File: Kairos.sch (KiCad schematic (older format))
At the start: 37 parts, among them U1 ATMEGA32U2-AU

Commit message: LED portion of main matrix, bug fixes
Add junctions which need to exist
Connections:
- net LEDGND: now reaches Q?.2 (C)
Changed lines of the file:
@@
 	0    1    1    0
 $EndComp
+Wire Wire Line
+	3850 1400 3850 1500
+Text GLabel 3850 1500 0    60   Input ~ 0
+LEDGND
 $EndSCHEMATC

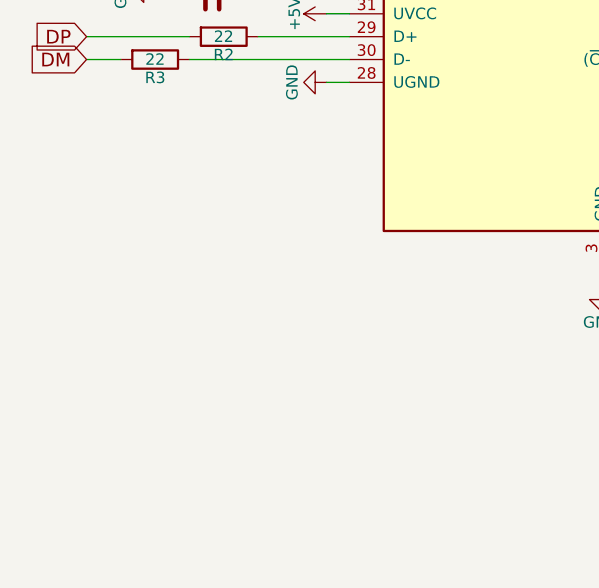
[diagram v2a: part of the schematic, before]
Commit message: Add USB
USB connector and PTC fuse for 5V
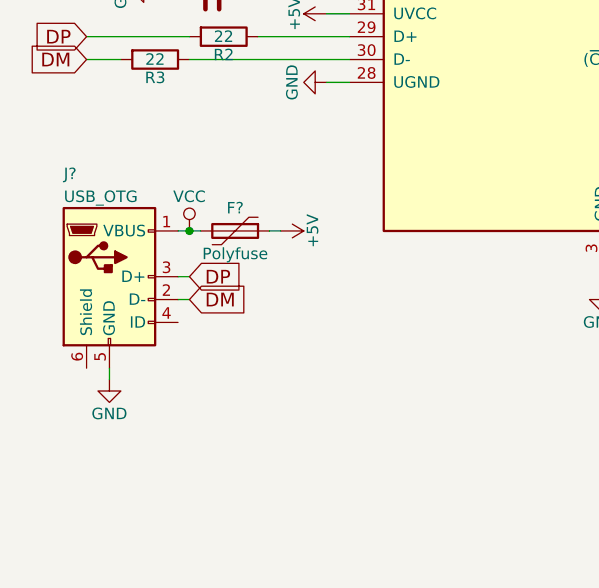
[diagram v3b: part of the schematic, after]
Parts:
- added F?: Polyfuse, symbol Polyfuse
- added J?: USB_OTG, symbol USB_OTG
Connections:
- net +5V: now also F?.1
- net DM: now also J?.2 (D-)
- net DP: now also J?.3 (D+)
- net GND: now also J?.5 (GND)
- new net VCC: F?.2, J?.1 (VBUS)
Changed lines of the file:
@@
 Text GLabel 3850 1500 0    60   Input ~ 0
 LEDGND
+$Comp
+L USB_OTG J?
+U 1 1 594639AC
+P 900 4500
+F 0 "J?" H 700 4950 50  0000 L CNN
+F 1 "USB_OTG" H 700 4850 50  0000 L CNN
+F 2 "" H 1050 4450 50  0001 C CNN
+F 3 "" H 1050 4450 50  0001 C CNN
+	1    900  4500
+	1    0    0    -1
+$EndComp
+$Comp
+L VCC #PWR?
+U 1 1 59465485
+P 1250 4300
+F 0 "#PWR?" H 1250 4150 50  0001 C CNN
+F 1 "VCC" H 1250 4450 50  0000 C CNN
+F 2 "" H 1250 4300 50  0001 C CNN
+F 3 "" H 1250 4300 50  0001 C CNN
+	1    1250 4300
+	1    0    0    -1
+$EndComp
+Wire Wire Line
+	1200 4300 1300 4300
+$Comp
+L Polyfuse F?
+U 1 1 5946558C
+P 1450 4300
+F 0 "F?" V 1350 4300 50  0000 C CNN
+F 1 "Polyfuse" V 1550 4300 50  0000 C CNN
+F 2 "" H 1500 4100 50  0001 L CNN
+F 3 "" H 1450 4300 50  0001 C CNN
+	1    1450 4300
+	0    1    1    0
+$EndComp
+Connection ~ 1250 4300
+Wire Wire Line
+	1600 4300 1650 4300
+$Comp
+L +5V #PWR?
+U 1 1 59465754
+P 1650 4300
+F 0 "#PWR?" H 1650 4150 50  0001 C CNN
+F 1 "+5V" H 1650 4440 50  0000 C CNN
+F 2 "" H 1650 4300 50  0001 C CNN
+F 3 "" H 1650 4300 50  0001 C CNN
+	1    1650 4300
+	0    1    1    0
+$EndComp
+Wire Wire Line
+	1200 4500 1250 4500
+Wire Wire Line
+	1200 4600 1250 4600
+Wire Wire Line
+	900  4900 900  4950
+$Comp
+L GND #PWR?
+U 1 1 594659E2
+P 900 4950
+F 0 "#PWR?" H 900 4700 50  0001 C CNN
+F 1 "GND" H 900 4800 50  0000 C CNN
+F 2 "" H 900 4950 50  0001 C CNN
+F 3 "" H 900 4950 50  0001 C CNN
+	1    900  4950
+	1    0    0    -1
+$EndComp
+Text GLabel 1250 4500 2    60   Input ~ 0
+DP
+Text GLabel 1250 4600 2    60   Input ~ 0
+DM
 $EndSCHEMATC

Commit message: Update annotations
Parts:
- gave numbers to parts that had none: 15
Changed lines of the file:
@@
 $EndComp
 $Comp
-L GND #PWR?
+L GND #PWR01
 U 1 1 5918DBD0
 P 1100 3250
-F 0 "#PWR?" H 1100 3000 50  0001 C CNN
+F 0 "#PWR01" H 1100 3000 50  0001 C CNN
 F 1 "GND" H 1100 3100 50  0000 C CNN
 F 2 "" H 1100 3250 50  0001 C CNN
@@
 $EndComp
 $Comp
-L +5V #PWR?
+L +5V #PWR02
 U 1 1 5918DF71
 P 1850 3350
-F 0 "#PWR?" H 1850 3200 50  0001 C CNN
+F 0 "#PWR02" H 1850 3200 50  0001 C CNN
 F 1 "+5V" H 1850 3490 50  0000 C CNN
 F 2 "" H 1850 3350 50  0001 C CNN
@@
 $EndComp
 $Comp
-L +5V #PWR?
+L +5V #PWR03
 U 1 1 5918E0B6
 P 1850 2450
-F 0 "#PWR?" H 1850 2300 50  0001 C CNN
+F 0 "#PWR03" H 1850 2300 50  0001 C CNN
 F 1 "+5V" H 1850 2590 50  0000 C CNN
 F 2 "" H 1850 2450 50  0001 C CNN
@@
 $EndComp
 $Comp
-L +5V #PWR?
+L +5V #PWR04
 U 1 1 5918E1F7
 P 3050 1550
-F 0 "#PWR?" H 3050 1400 50  0001 C CNN
+F 0 "#PWR04" H 3050 1400 50  0001 C CNN
 F 1 "+5V" H 3050 1690 50  0000 C CNN
 F 2 "" H 3050 1550 50  0001 C CNN
@@
 $EndComp
 $Comp
-L GND #PWR?
+L GND #PWR05
 U 1 1 5918E4E7
 P 1850 3650
-F 0 "#PWR?" H 1850 3400 50  0001 C CNN
+F 0 "#PWR05" H 1850 3400 50  0001 C CNN
 F 1 "GND" H 1850 3500 50  0000 C CNN
 F 2 "" H 1850 3650 50  0001 C CNN
@@
 $EndComp
 $Comp
-L GND #PWR?
+L GND #PWR06
 U 1 1 5918E5DF
 P 3050 4550
-F 0 "#PWR?" H 3050 4300 50  0001 C CNN
+F 0 "#PWR06" H 3050 4300 50  0001 C CNN
 F 1 "GND" H 3050 4400 50  0000 C CNN
 F 2 "" H 3050 4550 50  0001 C CNN
@@
 $EndComp
 $Comp
-L GND #PWR?
+L GND #PWR07
 U 1 1 5918EBA1
 P 1150 2350
-F 0 "#PWR?" H 1150 2100 50  0001 C CNN
+F 0 "#PWR07" H 1150 2100 50  0001 C CNN
 F 1 "GND" H 1150 2200 50  0000 C CNN
 F 2 "" H 1150 2350 50  0001 C CNN
@@
 $EndComp
 $Comp
-L GND #PWR?
+L GND #PWR08
 U 1 1 5918EEAC
 P 4650 3550
-F 0 "#PWR?" H 4650 3300 50  0001 C CNN
+F 0 "#PWR08" H 4650 3300 50  0001 C CNN
 F 1 "GND" H 4650 3400 50  0000 C CNN
 F 2 "" H 4650 3550 50  0001 C CNN
@@
 $EndComp
 $Comp
-L +5V #PWR?
+L +5V #PWR09
 U 1 1 5919016B
 P 1350 1500
-F 0 "#PWR?" H 1350 1350 50  0001 C CNN
+F 0 "#PWR09" H 1350 1350 50  0001 C CNN
 F 1 "+5V" H 1350 1640 50  0000 C CNN
 F 2 "" H 1350 1500 50  0001 C CNN
@@
 $EndComp
 $Comp
-L GND #PWR?
+L GND #PWR010
 U 1 1 59190191
 P 1350 2000
-F 0 "#PWR?" H 1350 1750 50  0001 C CNN
+F 0 "#PWR010" H 1350 1750 50  0001 C CNN
 F 1 "GND" H 1350 1850 50  0000 C CNN
 F 2 "" H 1350 2000 50  0001 C CNN
@@
 $EndComp
 $Comp
-L GND #PWR?
+L GND #PWR011
 U 1 1 59191048
 P 750 2700
-F 0 "#PWR?" H 750 2450 50  0001 C CNN
+F 0 "#PWR011" H 750 2450 50  0001 C CNN
 F 1 "GND" H 750 2550 50  0000 C CNN
 F 2 "" H 750 2700 50  0001 C CNN
@@
 $EndComp
 $Comp
-L BCP51 Q?
+L BCP51 Q1
 U 1 1 591916D1
 P 3950 1200
-F 0 "Q?" H 4150 1275 50  0000 L CNN
+F 0 "Q1" H 4150 1275 50  0000 L CNN
 F 1 "NSS40301MZ4T1G" H 4150 1200 50  0000 L CNN
 F 2 "TO_SOT_Packages_SMD:SOT-223" H 4150 1125 50  0001 L CIN
@@
 $EndComp
 $Comp
-L GND #PWR?
+L GND #PWR012
 U 1 1 59191F20
 P 3850 900
-F 0 "#PWR?" H 3850 650 50  0001 C CNN
+F 0 "#PWR012" H 3850 650 50  0001 C CNN
 F 1 "GND" H 3850 750 50  0000 C CNN
 F 2 "" H 3850 900 50  0001 C CNN
@@
 $EndComp
 $Comp
-L +5V #PWR?
+L +5V #PWR013
 U 1 1 59196108
 P 8500 850
-F 0 "#PWR?" H 8500 700 50  0001 C CNN
+F 0 "#PWR013" H 8500 700 50  0001 C CNN
 F 1 "+5V" H 8500 990 50  0000 C CNN
 F 2 "" H 8500 850 50  0001 C CNN
@@
 $EndComp
 $Comp
-L GND #PWR?
+L GND #PWR014
 U 1 1 5919672A
 P 9600 850
-F 0 "#PWR?" H 9600 600 50  0001 C CNN
+F 0 "#PWR014" H 9600 600 50  0001 C CNN
 F 1 "GND" H 9600 700 50  0000 C CNN
 F 2 "" H 9600 850 50  0001 C CNN
@@
 	9950 850  9950 5750
 $Comp
-L +5V #PWR?
+L +5V #PWR015
 U 1 1 59197C26
 P 9950 850
-F 0 "#PWR?" H 9950 700 50  0001 C CNN
+F 0 "#PWR015" H 9950 700 50  0001 C CNN
 F 1 "+5V" H 9950 990 50  0000 C CNN
 F 2 "" H 9950 850 50  0001 C CNN
@@
 	11050 1400 11000 1400
 $Comp
-L GND #PWR?
+L GND #PWR016
 U 1 1 591994C3
 P 11050 850
-F 0 "#PWR?" H 11050 600 50  0001 C CNN
+F 0 "#PWR016" H 11050 600 50  0001 C CNN
 F 1 "GND" H 11050 700 50  0000 C CNN
 F 2 "" H 11050 850 50  0001 C CNN
@@
 $EndSheet
 $Comp
-L C CR?
+L C CR1
 U 1 1 5919EB18
 P 6350 5400
-F 0 "CR?" H 6375 5500 50  0000 L CNN
+F 0 "CR1" H 6375 5500 50  0000 L CNN
 F 1 "100nF" H 6375 5300 50  0000 L CNN
 F 2 "" H 6388 5250 50  0001 C CNN
@@
 $EndComp
 $Comp
-L C CR?
+L C CR2
 U 1 1 5919FDAD
 P 6650 5400
-F 0 "CR?" H 6675 5500 50  0000 L CNN
+F 0 "CR2" H 6675 5500 50  0000 L CNN
 F 1 "100nF" H 6675 5300 50  0000 L CNN
 F 2 "" H 6688 5250 50  0001 C CNN
@@
 $EndComp
 $Comp
-L C CR?
+L C CR3
 U 1 1 5919FE22
 P 6950 5400
-F 0 "CR?" H 6975 5500 50  0000 L CNN
+F 0 "CR3" H 6975 5500 50  0000 L CNN
 F 1 "100nF" H 6975 5300 50  0000 L CNN
 F 2 "" H 6988 5250 50  0001 C CNN
@@
 $EndComp
 $Comp
-L C CR?
+L C CR4
 U 1 1 5919FE8E
 P 7250 5400
-F 0 "CR?" H 7275 5500 50  0000 L CNN
+F 0 "CR4" H 7275 5500 50  0000 L CNN
 F 1 "100nF" H 7275 5300 50  0000 L CNN
 F 2 "" H 7288 5250 50  0001 C CNN
@@
 $EndComp
 $Comp
-L C CR?
+L C CR5
 U 1 1 591A01D2
 P 7550 5400
-F 0 "CR?" H 7575 5500 50  0000 L CNN
+F 0 "CR5" H 7575 5500 50  0000 L CNN
 F 1 "100nF" H 7575 5300 50  0000 L CNN
 F 2 "" H 7588 5250 50  0001 C CNN
@@
 $EndComp
 $Comp
-L C CR?
+L C CR6
 U 1 1 591A0284
 P 7850 5400
-F 0 "CR?" H 7875 5500 50  0000 L CNN
+F 0 "CR6" H 7875 5500 50  0000 L CNN
 F 1 "100nF" H 7875 5300 50  0000 L CNN
 F 2 "" H 7888 5250 50  0001 C CNN
@@
 	7850 5550 6200 5550
 $Comp
-L +5V #PWR?
+L +5V #PWR017
 U 1 1 591A0912
 P 6200 5250
-F 0 "#PWR?" H 6200 5100 50  0001 C CNN
+F 0 "#PWR017" H 6200 5100 50  0001 C CNN
 F 1 "+5V" H 6200 5390 50  0000 C CNN
 F 2 "" H 6200 5250 50  0001 C CNN
@@
 $EndComp
 $Comp
-L GND #PWR?
+L GND #PWR018
 U 1 1 591A09A2
 P 6200 5550
-F 0 "#PWR?" H 6200 5300 50  0001 C CNN
+F 0 "#PWR018" H 6200 5300 50  0001 C CNN
 F 1 "GND" H 6200 5400 50  0000 C CNN
 F 2 "" H 6200 5550 50  0001 C CNN
@@
 $EndComp
 $Comp
-L C CR?
+L C CR7
 U 1 1 591A0E23
 P 6350 5900
-F 0 "CR?" H 6375 6000 50  0000 L CNN
+F 0 "CR7" H 6375 6000 50  0000 L CNN
 F 1 "100nF" H 6375 5800 50  0000 L CNN
 F 2 "" H 6388 5750 50  0001 C CNN
@@
 $EndComp
 $Comp
-L C CR?
+L C CR8
 U 1 1 591A0E29
 P 6650 5900
-F 0 "CR?" H 6675 6000 50  0000 L CNN
+F 0 "CR8" H 6675 6000 50  0000 L CNN
 F 1 "100nF" H 6675 5800 50  0000 L CNN
 F 2 "" H 6688 5750 50  0001 C CNN
@@
 $EndComp
 $Comp
-L C CR?
+L C CR9
 U 1 1 591A0E2F
 P 6950 5900
-F 0 "CR?" H 6975 6000 50  0000 L CNN
+F 0 "CR9" H 6975 6000 50  0000 L CNN
 F 1 "100nF" H 6975 5800 50  0000 L CNN
 F 2 "" H 6988 5750 50  0001 C CNN
@@
 $EndComp
 $Comp
-L C CR?
+L C CR10
 U 1 1 591A0E35
 P 7250 5900
-F 0 "CR?" H 7275 6000 50  0000 L CNN
+F 0 "CR10" H 7275 6000 50  0000 L CNN
 F 1 "100nF" H 7275 5800 50  0000 L CNN
 F 2 "" H 7288 5750 50  0001 C CNN
@@
 $EndComp
 $Comp
-L C CR?
+L C CR11
 U 1 1 591A0E3B
 P 7550 5900
-F 0 "CR?" H 7575 6000 50  0000 L CNN
+F 0 "CR11" H 7575 6000 50  0000 L CNN
 F 1 "100nF" H 7575 5800 50  0000 L CNN
 F 2 "" H 7588 5750 50  0001 C CNN
@@
 $EndComp
 $Comp
-L C CR?
+L C CR12
 U 1 1 591A0E41
 P 7850 5900
-F 0 "CR?" H 7875 6000 50  0000 L CNN
+F 0 "CR12" H 7875 6000 50  0000 L CNN
 F 1 "100nF" H 7875 5800 50  0000 L CNN
 F 2 "" H 7888 5750 50  0001 C CNN
@@
 	7850 6050 6200 6050
 $Comp
-L +5V #PWR?
+L +5V #PWR019
 U 1 1 591A0E49
 P 6200 5750
-F 0 "#PWR?" H 6200 5600 50  0001 C CNN
+F 0 "#PWR019" H 6200 5600 50  0001 C CNN
 F 1 "+5V" H 6200 5890 50  0000 C CNN
 F 2 "" H 6200 5750 50  0001 C CNN
@@
 $EndComp
 $Comp
-L GND #PWR?
+L GND #PWR020
 U 1 1 591A0E4F
 P 6200 6050
-F 0 "#PWR?" H 6200 5800 50  0001 C CNN
+F 0 "#PWR020" H 6200 5800 50  0001 C CNN
 F 1 "GND" H 6200 5900 50  0000 C CNN
 F 2 "" H 6200 6050 50  0001 C CNN
@@
 LEDGND
 $Comp
-L USB_OTG J?
+L USB_OTG J1
 U 1 1 594639AC
 P 900 4500
-F 0 "J?" H 700 4950 50  0000 L CNN
+F 0 "J1" H 700 4950 50  0000 L CNN
 F 1 "USB_OTG" H 700 4850 50  0000 L CNN
 F 2 "" H 1050 4450 50  0001 C CNN
@@
 $EndComp
 $Comp
-L VCC #PWR?
+L VCC #PWR021
 U 1 1 59465485
 P 1250 4300
-F 0 "#PWR?" H 1250 4150 50  0001 C CNN
+F 0 "#PWR021" H 1250 4150 50  0001 C CNN
 F 1 "VCC" H 1250 4450 50  0000 C CNN
 F 2 "" H 1250 4300 50  0001 C CNN
@@
 	1200 4300 1300 4300
 $Comp
-L Polyfuse F?
+L Polyfuse F1
 U 1 1 5946558C
 P 1450 4300
-F 0 "F?" V 1350 4300 50  0000 C CNN
+F 0 "F1" V 1350 4300 50  0000 C CNN
 F 1 "Polyfuse" V 1550 4300 50  0000 C CNN
 F 2 "" H 1500 4100 50  0001 L CNN
@@
 	1600 4300 1650 4300
 $Comp
-L +5V #PWR?
+L +5V #PWR022
 U 1 1 59465754
 P 1650 4300
-F 0 "#PWR?" H 1650 4150 50  0001 C CNN
+F 0 "#PWR022" H 1650 4150 50  0001 C CNN
 F 1 "+5V" H 1650 4440 50  0000 C CNN
 F 2 "" H 1650 4300 50  0001 C CNN
@@
 	900  4900 900  4950
 $Comp
-L GND #PWR?
+L GND #PWR023
 U 1 1 594659E2
 P 900 4950
-F 0 "#PWR?" H 900 4700 50  0001 C CNN
+F 0 "#PWR023" H 900 4700 50  0001 C CNN
 F 1 "GND" H 900 4800 50  0000 C CNN
 F 2 "" H 900 4950 50  0001 C CNN

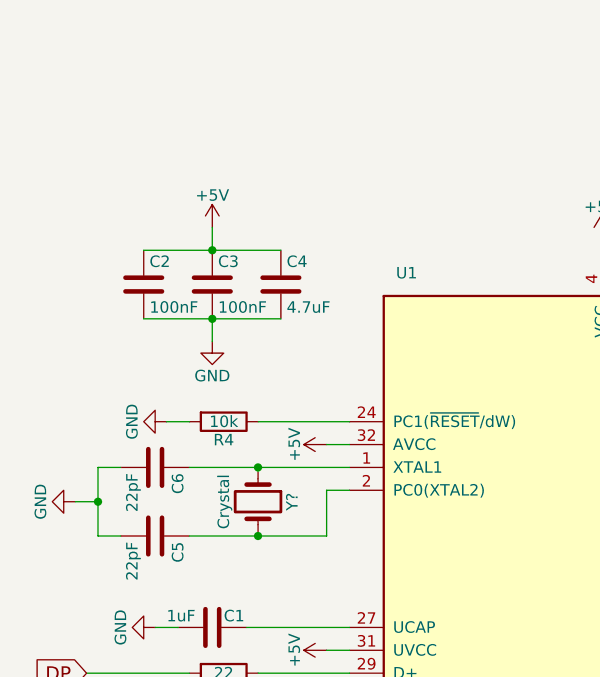
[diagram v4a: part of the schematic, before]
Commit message: Add reset button, link libs
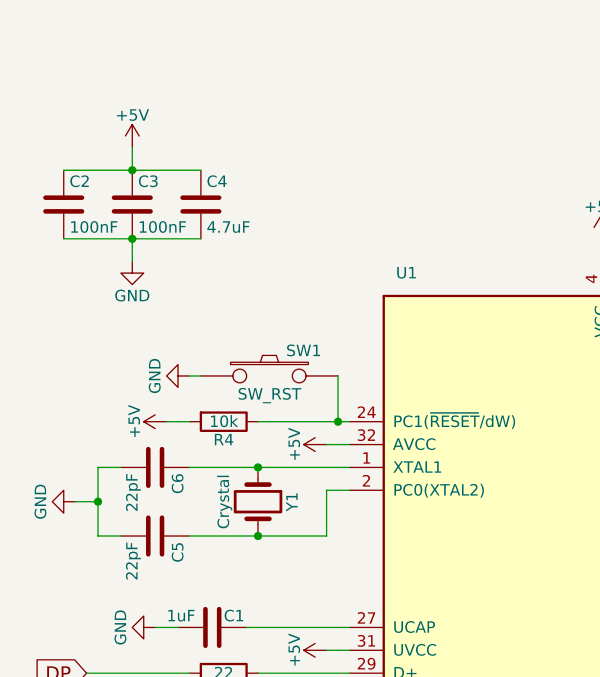
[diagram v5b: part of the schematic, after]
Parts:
- added SW1: SW_RST, symbol SW_PUSH
- gave numbers to parts that had none: 1
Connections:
- net +5V: now also R4.2
- net GND: now also SW1.1; no longer R4.2
- net at R4.1, U1.24 (PC1(~RESET~/dW)): now also SW1.2
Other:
- moved on the sheet: C2, C3, C4
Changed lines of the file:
@@
 LIBS:MX_Alps_Hybrids
 LIBS:ws2812b
+LIBS:keyboard_parts
 LIBS:Kairos-cache
 EELAYER 25 0
@@
 $EndComp
 $Comp
-L GND #PWR07
-U 1 1 5918EBA1
-P 1150 2350
-F 0 "#PWR07" H 1150 2100 50  0001 C CNN
-F 1 "GND" H 1150 2200 50  0000 C CNN
-F 2 "" H 1150 2350 50  0001 C CNN
-F 3 "" H 1150 2350 50  0001 C CNN
-	1    1150 2350
-	0    1    1    0
-$EndComp
-$Comp
 L GND #PWR08
 U 1 1 5918EEAC
@@
 L C C2
 U 1 1 5918F5AF
-P 1050 1750
-F 0 "C2" H 1075 1850 50  0000 L CNN
-F 1 "100nF" H 1075 1650 50  0000 L CNN
-F 2 "" H 1088 1600 50  0001 C CNN
-F 3 "" H 1050 1750 50  0001 C CNN
-	1    1050 1750
+P 700 1400
+F 0 "C2" H 725 1500 50  0000 L CNN
+F 1 "100nF" H 725 1300 50  0000 L CNN
+F 2 "" H 738 1250 50  0001 C CNN
+F 3 "" H 700 1400 50  0001 C CNN
+	1    700  1400
 	1    0    0    -1
 $EndComp
@@
 L C C3
 U 1 1 5918F6D8
-P 1350 1750
-F 0 "C3" H 1375 1850 50  0000 L CNN
-F 1 "100nF" H 1375 1650 50  0000 L CNN
-F 2 "" H 1388 1600 50  0001 C CNN
-F 3 "" H 1350 1750 50  0001 C CNN
-	1    1350 1750
+P 1000 1400
+F 0 "C3" H 1025 1500 50  0000 L CNN
+F 1 "100nF" H 1025 1300 50  0000 L CNN
+F 2 "" H 1038 1250 50  0001 C CNN
+F 3 "" H 1000 1400 50  0001 C CNN
+	1    1000 1400
 	1    0    0    -1
 $EndComp
@@
 L C C4
 U 1 1 5918F707
-P 1650 1750
-F 0 "C4" H 1675 1850 50  0000 L CNN
-F 1 "4.7uF" H 1675 1650 50  0000 L CNN
-F 2 "" H 1688 1600 50  0001 C CNN
-F 3 "" H 1650 1750 50  0001 C CNN
-	1    1650 1750
+P 1300 1400
+F 0 "C4" H 1325 1500 50  0000 L CNN
+F 1 "4.7uF" H 1325 1300 50  0000 L CNN
+F 2 "" H 1338 1250 50  0001 C CNN
+F 3 "" H 1300 1400 50  0001 C CNN
+	1    1300 1400
 	1    0    0    -1
 $EndComp
@@
 L +5V #PWR09
 U 1 1 5919016B
-P 1350 1500
-F 0 "#PWR09" H 1350 1350 50  0001 C CNN
-F 1 "+5V" H 1350 1640 50  0000 C CNN
-F 2 "" H 1350 1500 50  0001 C CNN
-F 3 "" H 1350 1500 50  0001 C CNN
-	1    1350 1500
+P 1000 1150
+F 0 "#PWR09" H 1000 1000 50  0001 C CNN
+F 1 "+5V" H 1000 1290 50  0000 C CNN
+F 2 "" H 1000 1150 50  0001 C CNN
+F 3 "" H 1000 1150 50  0001 C CNN
+	1    1000 1150
 	1    0    0    -1
 $EndComp
@@
 L GND #PWR010
 U 1 1 59190191
-P 1350 2000
-F 0 "#PWR010" H 1350 1750 50  0001 C CNN
-F 1 "GND" H 1350 1850 50  0000 C CNN
-F 2 "" H 1350 2000 50  0001 C CNN
-F 3 "" H 1350 2000 50  0001 C CNN
-	1    1350 2000
-	1    0    0    -1
-$EndComp
-$Comp
-L Crystal Y?
+P 1000 1650
+F 0 "#PWR010" H 1000 1400 50  0001 C CNN
+F 1 "GND" H 1000 1500 50  0000 C CNN
+F 2 "" H 1000 1650 50  0001 C CNN
+F 3 "" H 1000 1650 50  0001 C CNN
+	1    1000 1650
+	1    0    0    -1
+$EndComp
+$Comp
+L Crystal Y1
 U 1 1 59190D6E
 P 1550 2700
-F 0 "Y?" H 1550 2850 50  0000 C CNN
+F 0 "Y1" H 1550 2850 50  0000 C CNN
 F 1 "Crystal" H 1550 2550 50  0000 C CNN
 F 2 "" H 1550 2700 50  0001 C CNN
@@
 	4550 3550 4650 3550
 Wire Wire Line
-	1050 1600 1650 1600
-Connection ~ 1350 1600
-Wire Wire Line
-	1050 1900 1650 1900
-Connection ~ 1350 1900
-Wire Wire Line
-	1350 1600 1350 1500
-Wire Wire Line
-	1350 1900 1350 2000
+	700  1250 1300 1250
+Connection ~ 1000 1250
+Wire Wire Line
+	700  1550 1300 1550
+Connection ~ 1000 1550
+Wire Wire Line
+	1000 1250 1000 1150
+Wire Wire Line
+	1000 1550 1000 1650
 Wire Wire Line
 	1250 2550 1950 2550
@@
 Text GLabel 1250 4600 2    60   Input ~ 0
 DM
+$Comp
+L SW_PUSH SW1
+U 1 1 59462D09
+P 1600 2150
+F 0 "SW1" H 1750 2260 50  0000 C CNN
+F 1 "SW_RST" H 1600 2070 50  0000 C CNN
+F 2 "" H 1600 2150 60  0000 C CNN
+F 3 "" H 1600 2150 60  0000 C CNN
+	1    1600 2150
+	1    0    0    -1
+$EndComp
+Wire Wire Line
+	1900 2150 1900 2350
+Connection ~ 1900 2350
+Wire Wire Line
+	1300 2150 1250 2150
+$Comp
+L GND #PWR?
+U 1 1 594641E8
+P 1250 2150
+F 0 "#PWR?" H 1250 1900 50  0001 C CNN
+F 1 "GND" H 1250 2000 50  0000 C CNN
+F 2 "" H 1250 2150 50  0001 C CNN
+F 3 "" H 1250 2150 50  0001 C CNN
+	1    1250 2150
+	0    1    1    0
+$EndComp
+$Comp
+L +5V #PWR?
+U 1 1 59464275
+P 1150 2350
+F 0 "#PWR?" H 1150 2200 50  0001 C CNN
+F 1 "+5V" H 1150 2490 50  0000 C CNN
+F 2 "" H 1150 2350 50  0001 C CNN
+F 3 "" H 1150 2350 50  0001 C CNN
+	1    1150 2350
+	0    -1   -1   0
+$EndComp
 $EndSCHEMATC

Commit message: Some minor edits
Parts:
- SW1: value SW_RST -> SW_RST1
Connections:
- no-connect marks 0 -> 2

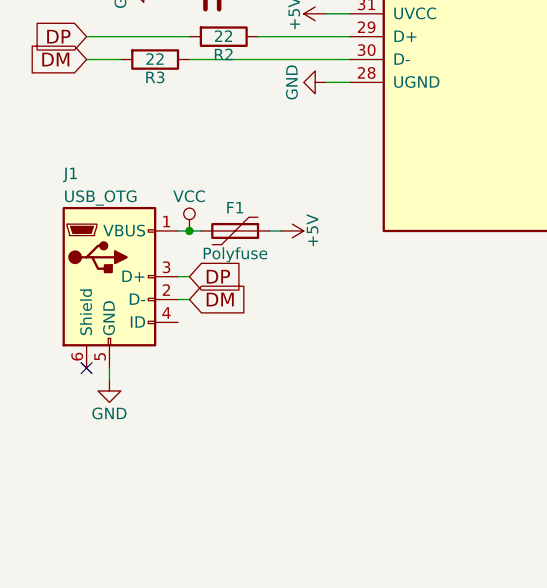
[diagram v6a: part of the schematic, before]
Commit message: Swap USB connector lib
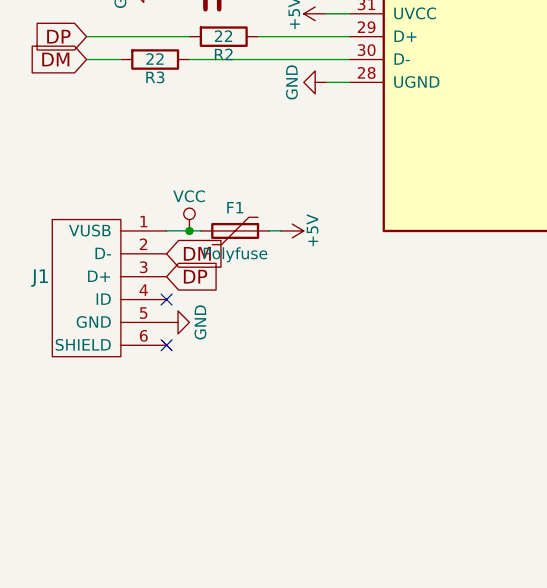
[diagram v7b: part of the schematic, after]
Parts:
- removed J1: USB_OTG, symbol USB_OTG
- added J1: USB_mini_micro_B, symbol USB_mini_micro_B
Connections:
- net DM: now also J1.2 (D-)
- net DP: now also J1.3 (D+)
- net GND: now also J1.5 (GND)
- net VCC: now also J1.1 (VUSB)
- no-connect marks 2 -> 3
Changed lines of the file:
@@
 LEDGND
-$Comp
-L USB_OTG J1
-U 1 1 594639AC
-P 900 4500
-F 0 "J1" H 700 4950 50  0000 L CNN
-F 1 "USB_OTG" H 700 4850 50  0000 L CNN
-F 2 "" H 1050 4450 50  0001 C CNN
-F 3 "" H 1050 4450 50  0001 C CNN
-	1    900  4500
-	1    0    0    -1
-$EndComp
 $Comp
 L VCC #PWR020
@@
 L GND #PWR022
 U 1 1 594659E2
-P 900 4950
-F 0 "#PWR022" H 900 4700 50  0001 C CNN
-F 1 "GND" H 900 4800 50  0000 C CNN
-F 2 "" H 900 4950 50  0001 C CNN
-F 3 "" H 900 4950 50  0001 C CNN
-	1    900  4950
-	1    0    0    -1
-$EndComp
-Text GLabel 1250 4500 2    60   Input ~ 0
+P 1150 4700
+F 0 "#PWR022" H 1150 4450 50  0001 C CNN
+F 1 "GND" H 1150 4550 50  0000 C CNN
+F 2 "" H 1150 4700 50  0001 C CNN
+F 3 "" H 1150 4700 50  0001 C CNN
+	1    1150 4700
+	0    -1   -1   0
+$EndComp
+Text GLabel 1150 4500 2    60   Input ~ 0
 DP
-Text GLabel 1250 4600 2    60   Input ~ 0
+Text GLabel 1150 4400 2    60   Input ~ 0
 DM
 $Comp
@@
 	3850 1400 3850 1500
 Wire Wire Line
-	1200 4300 1300 4300
+	1150 4300 1300 4300
 Connection ~ 1250 4300
 Wire Wire Line
 	1600 4300 1650 4300
-Wire Wire Line
-	1200 4500 1250 4500
-Wire Wire Line
-	1200 4600 1250 4600
-Wire Wire Line
-	900  4900 900  4950
 Wire Wire Line
 	1900 2150 1900 2350
@@
 Wire Wire Line
 	1300 2150 1250 2150
-NoConn ~ 800  4900
 NoConn ~ 10000 6150
+$Comp
+L USB_mini_micro_B J1
+U 1 1 5947BA25
+P 1000 4450
+F 0 "J1" H 600 4400 60  0000 C CNN
+F 1 "USB_mini_micro_B" H 850 4700 60  0001 C CNN
+F 2 "" H 950 4450 60  0000 C CNN
+F 3 "" H 950 4450 60  0000 C CNN
+	1    1000 4450
+	1    0    0    -1
+$EndComp
+NoConn ~ 1150 4600
+NoConn ~ 1150 4800
 $EndSCHEMATC
